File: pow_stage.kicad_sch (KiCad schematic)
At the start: 53 parts, among them J10 I2C_Conn, J11 USB_C, J9 V_BATT, SW16 SW_Push_Dual, U1 MP3438GTL-P, U15 LTC2950CTS8-1-TRMPBF, U2 MP3421GG-Z, U3 LM1117DT-3.3, U4 MP2722GRH-0000-P

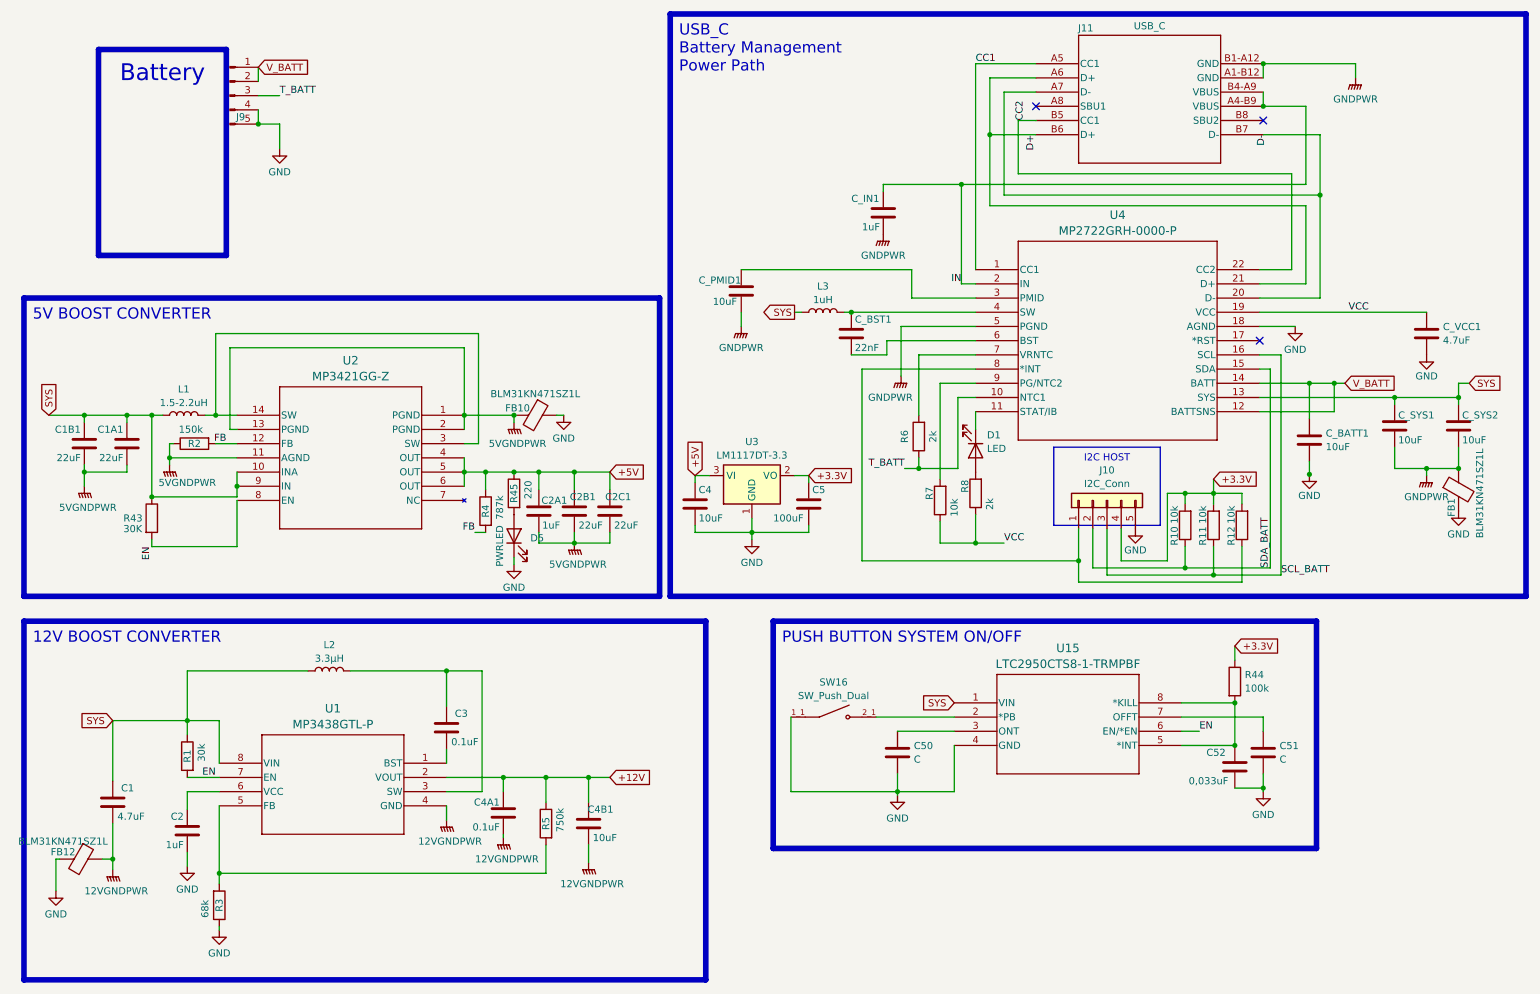
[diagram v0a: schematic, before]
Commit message: fix hdmi traces and push button kill pin supply
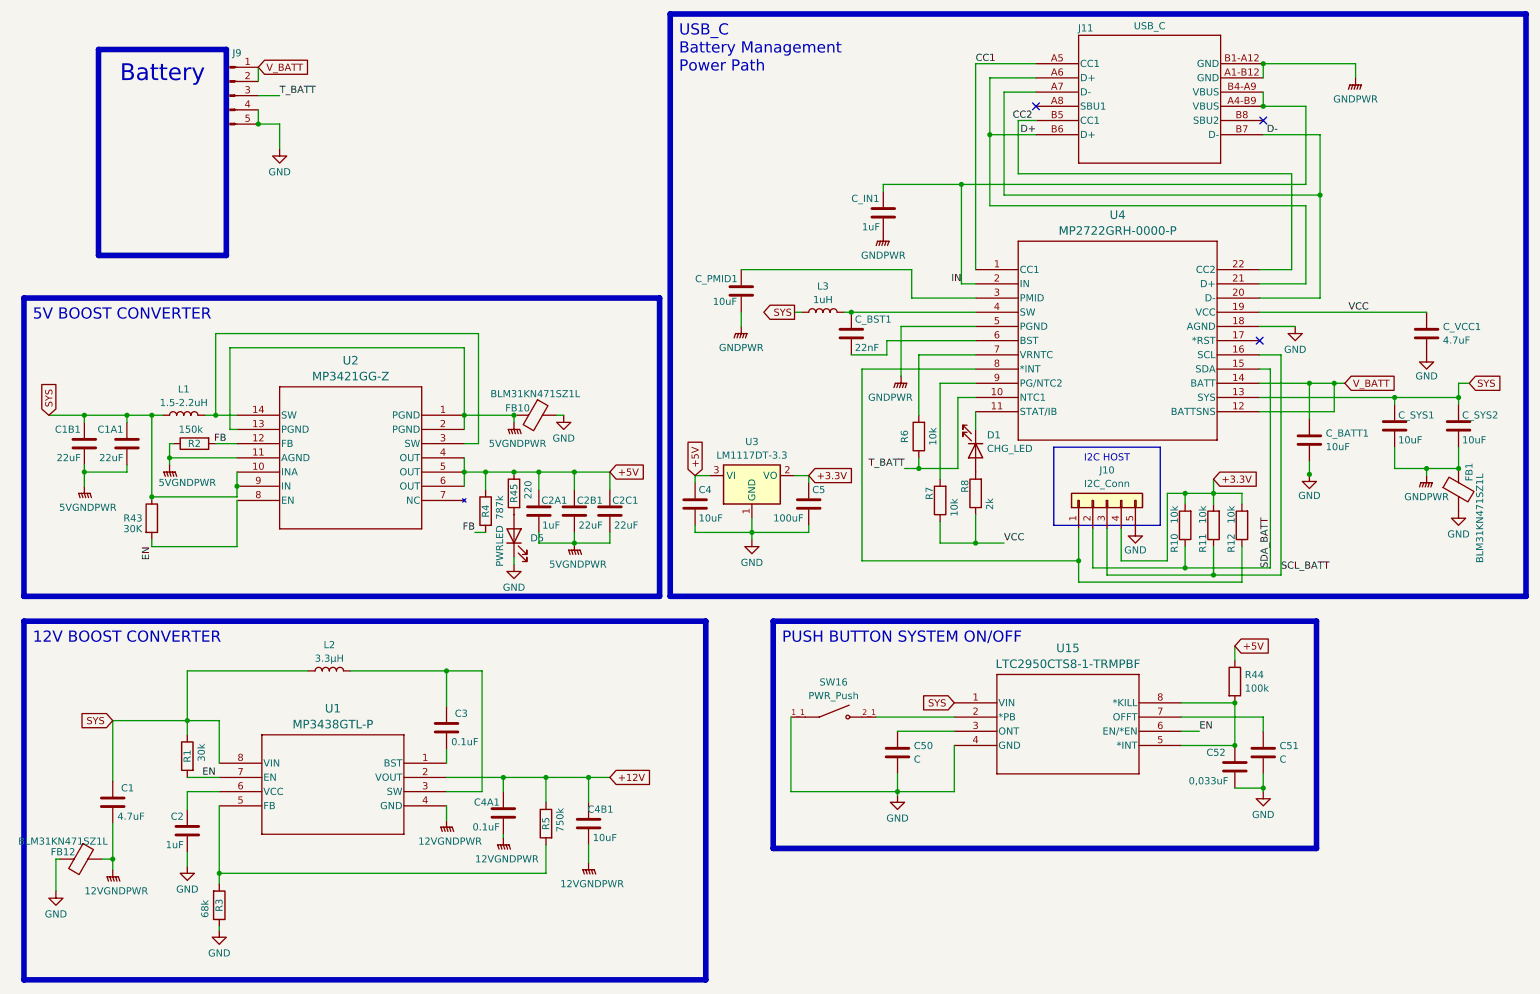
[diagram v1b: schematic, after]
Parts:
- D1: value LED -> CHG_LED
- R6: value 2k -> 10k
- SW16: value SW_Push_Dual -> PWR_Push
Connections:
- net +3.3V: no longer R44.1
- net +5V: now also R44.1
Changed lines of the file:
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@@
 	)
 	(label "CC2"
-		(at 193.675 32.385 90)
+		(at 194.945 32.385 180)
 		(fields_autoplaced yes)
 		(effects
@@
 				(size 1.27 1.27)
 			)
-			(justify left bottom)
+			(justify right bottom)
 		)
 	)
@@
 	)
 	(label "D-"
-		(at 236.855 34.925 270)
+		(at 236.855 34.925 0)
 		(fields_autoplaced yes)
 		(effects
@@
 				(size 1.27 1.27)
 			)
-			(justify right bottom)
+			(justify left bottom)
 		)
 	)
@@
 	)
 	(label "D+"
-		(at 195.58 34.925 270)
+		(at 195.58 34.925 180)
 		(fields_autoplaced yes)
 		(effects
@@
 	)
 	(label "SCL_BATT"
-		(at 239.395 113.665 0)
+		(at 239.395 113.03 0)
 		(fields_autoplaced yes)
 		(effects
@@
 		)
 	)
+	(global_label "+5V"
+		(shape input)
+		(at 231.14 126.365 0)
+		(fields_autoplaced yes)
+		(effects
+			(font
+				(size 1.27 1.27)
+			)
+			(justify left)
+		)
+		(property "Intersheetrefs" "${INTERSHEET_REFS}"
+			(at 237.9957 126.365 0)
+			(effects
+				(font
+					(size 1.27 1.27)
+				)
+				(justify left)
+				(hide yes)
+			)
+		)
+	)
 	(global_label "+3.3V"
 		(shape input)
@@
 		)
 	)
-	(global_label "+3.3V"
-		(shape input)
-		(at 231.14 126.365 0)
-		(fields_autoplaced yes)
-		(effects
-			(font
-				(size 1.27 1.27)
-			)
-			(justify left)
-		)
-		(property "Intersheetrefs" "${INTERSHEET_REFS}"
-			(at 239.81 126.365 0)
-			(effects
-				(font
-					(size 1.27 1.27)
-				)
-				(justify left)
-				(hide yes)
-			)
-		)
-	)
 	(global_label "SYS"
 		(shape input)
@@
 		(dnp no)
 		(property "Reference" "J9"
-			(at 53.34 31.75 0)
+			(at 52.705 20.32 0)
 			(effects
 				(font
@@
 		(dnp no)
 		(property "Reference" "R12"
-			(at 230.505 106.68 90)
+			(at 230.505 107.95 90)
 			(effects
 				(font
@@
 			)
 		)
-		(property "Value" "LED"
+		(property "Value" "CHG_LED"
 			(at 186.817 91.0646 90)
 			(effects
@@
 			)
 		)
-		(property "Value" "2k"
+		(property "Value" "10k"
 			(at 177.165 88.9 90)
 			(effects
@@
 		(dnp no)
 		(property "Reference" "C2B1"
-			(at 116.84 99.695 0)
+			(at 118.11 100.33 0)
 			(effects
 				(font
@@
 		(dnp no)
 		(property "Reference" "C2C1"
-			(at 123.19 99.695 0)
+			(at 124.46 100.33 0)
 			(effects
 				(font
@@
 			)
 		)
-		(property "Value" "SW_Push_Dual"
+		(property "Value" "PWR_Push"
 			(at 159.385 135.262 0)
 			(effects
@@
 		(dnp no)
 		(property "Reference" "R11"
-			(at 225.425 106.68 90)
+			(at 225.425 107.95 90)
 			(effects
 				(font
@@
 		(dnp no)
 		(property "Reference" "C_PMID1"
-			(at 135.255 60.96 0)
+			(at 134.62 60.706 0)
 			(effects
 				(font
@@
 		(dnp no)
 		(property "Reference" "R10"
-			(at 220.345 106.68 90)
+			(at 220.345 107.95 90)
 			(effects
 				(font
@@
 		(dnp no)
 		(property "Reference" "FB1"
-			(at 269.875 101.6 90)
+			(at 273.05 95.25 90)
 			(effects
 				(font
@@
 		)
 		(property "Value" "	BLM31KN471SZ1L"
-			(at 274.955 99.06 90)
+			(at 274.955 103.505 90)
 			(effects
 				(font

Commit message: update layout pcb & zip tesi
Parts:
- C50, C51: value C -> 0.033uF
- C52: value 0,033uF -> 0.01uF
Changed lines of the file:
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@@
 			)
 		)
-		(property "Value" "0,033uF"
-			(at 222.885 150.495 0)
+		(property "Value" "0.01uF"
+			(at 223.52 150.495 0)
 			(effects
 				(font
@@
 		(on_board yes)
 		(dnp no)
-		(fields_autoplaced yes)
 		(property "Reference" "C50"
-			(at 173.736 144.2028 0)
+			(at 171.45 142.875 0)
 			(effects
 				(font
@@
 			)
 		)
-		(property "Value" "C"
-			(at 173.736 146.6271 0)
+		(property "Value" "0.033uF"
+			(at 171.45 147.955 0)
 			(effects
 				(font
@@
 		(dnp no)
 		(property "Reference" "C4B1"
-			(at 120.015 155.575 0)
+			(at 121.285 155.575 0)
 			(effects
 				(font
@@
 		)
 		(property "Value" "	BLM31KN471SZ1L"
-			(at 21.59 161.29 90)
+			(at 20.955 160.655 90)
 			(effects
 				(font
-					(size 1.27 1.27)
+					(size 1 1)
 				)
 			)
@@
 		(dnp no)
 		(property "Reference" "C4A1"
-			(at 99.695 154.305 0)
+			(at 106.045 153.67 0)
 			(effects
 				(font
@@
 		)
 		(property "Value" "0.1uF"
-			(at 99.695 158.75 0)
+			(at 106.045 158.75 0)
 			(effects
 				(font
@@
 		(on_board yes)
 		(dnp no)
-		(fields_autoplaced yes)
 		(property "Reference" "C51"
-			(at 239.141 144.2028 0)
+			(at 236.855 142.875 0)
 			(effects
 				(font
@@
 			)
 		)
-		(property "Value" "C"
-			(at 239.141 146.6271 0)
+		(property "Value" "0.033uF"
+			(at 236.855 147.955 0)
 			(effects
 				(font
@@
 		(dnp no)
 		(property "Reference" "C3"
-			(at 93.98 138.43 0)
+			(at 93.345 138.43 0)
 			(effects
 				(font
@@
 		(dnp no)
 		(property "Reference" "C1"
-			(at 34.29 151.765 0)
+			(at 33.655 151.765 0)
 			(effects
 				(font
